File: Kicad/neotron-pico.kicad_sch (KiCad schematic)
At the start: 15 parts

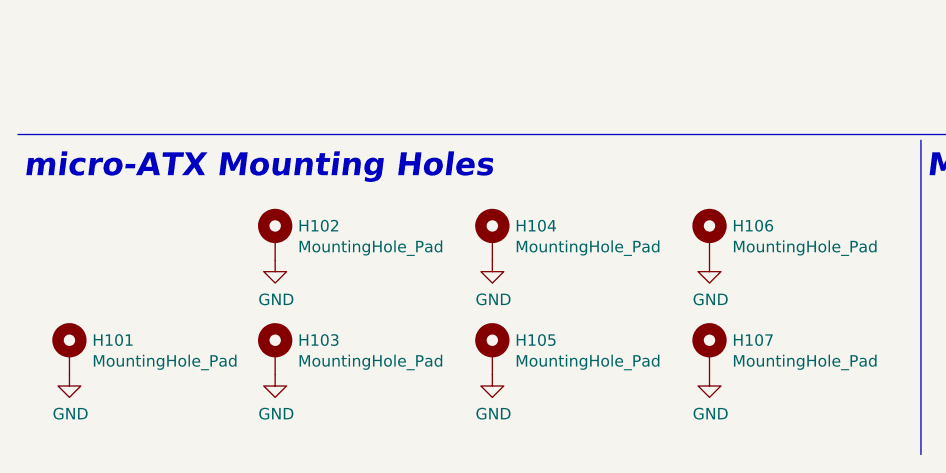
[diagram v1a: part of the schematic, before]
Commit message: Reworked audio circuit.
Based on TLV320AIC23B evaluation board. Removed Pi filters. Used SMD
electrolytic caps for headphone out.
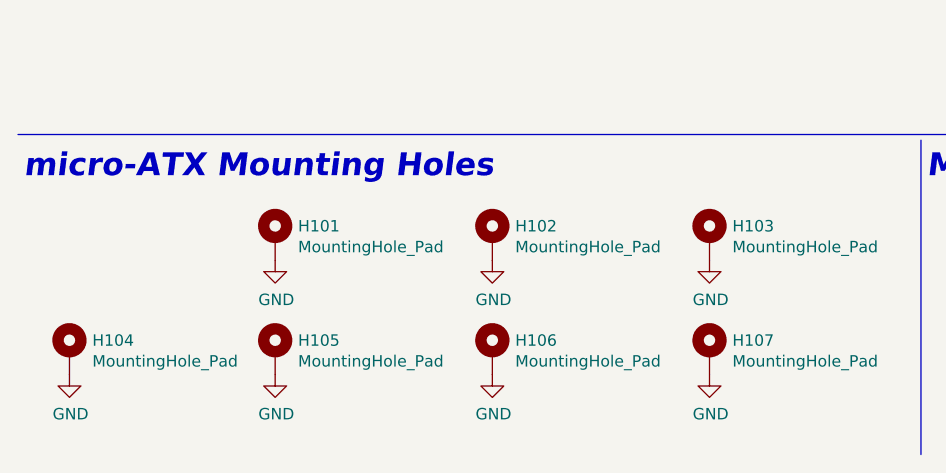
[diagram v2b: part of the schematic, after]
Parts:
- renumbered H102 to H101, H104 to H102, H106 to H103, H101 to H104, H103 to H105, H105 to H106

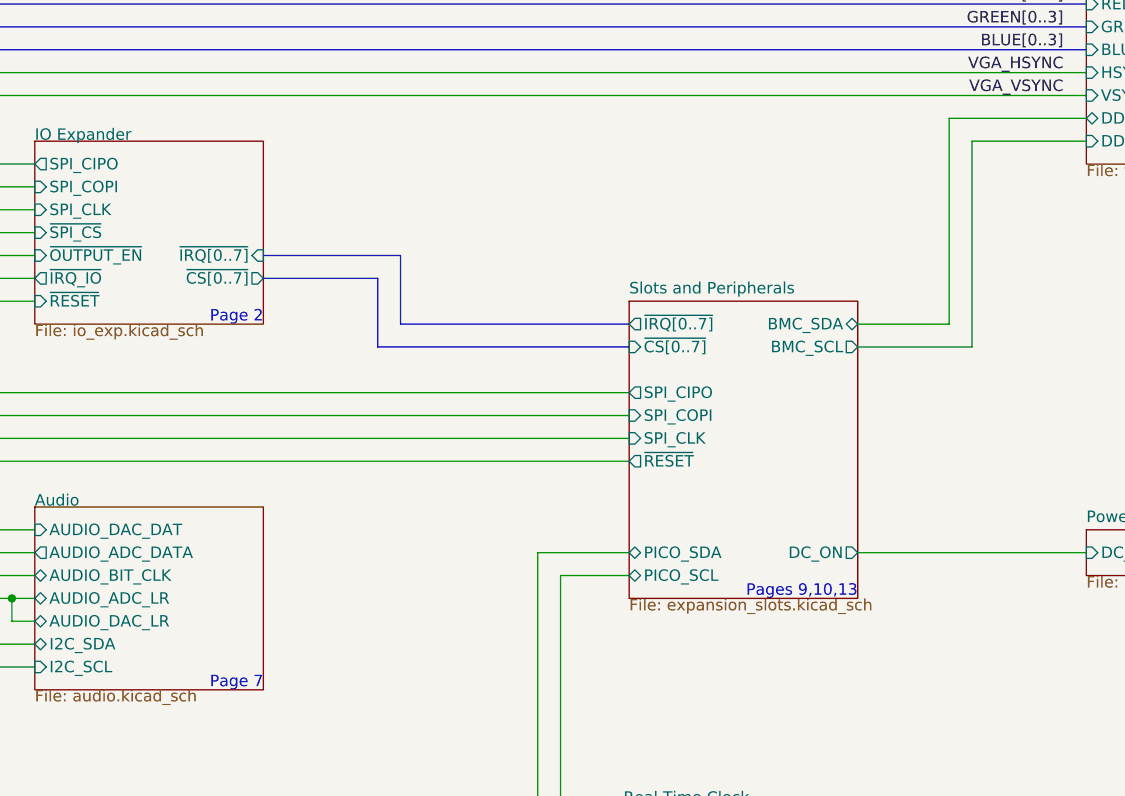
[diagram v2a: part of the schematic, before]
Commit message: Added a PC Speaker output.
To free up a BMC pin, the HDD LED is now driven from the I/O mux.
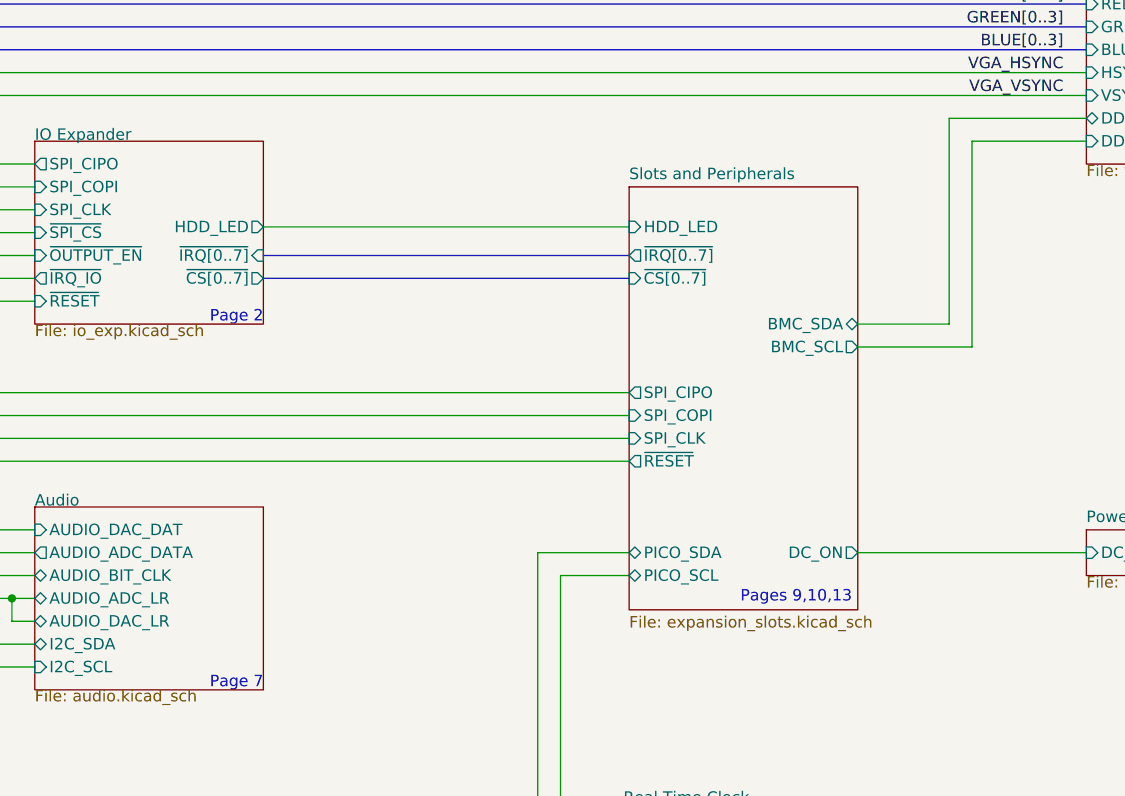
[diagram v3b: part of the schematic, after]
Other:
- sheet IO Expander ports: added HDD_LED; removed none
- sheet Slots and Peripherals ports: added HDD_LED; removed none

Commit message: Added source resistors on SPI bus.
Also renumbered pages.
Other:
- note added: "Page 13"
- note added: "Page 3"
- note added: "Pages 4-7"
- note added: "Pages 9-11"
- note removed: "Page 11"
- note removed: "Page 7"
- note removed: "Pages 3-6"
- note removed: "Pages 9,10,13"
